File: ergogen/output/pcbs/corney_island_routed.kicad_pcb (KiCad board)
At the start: 2 copper layers, 134.2 x 92.7 mm, 46 parts

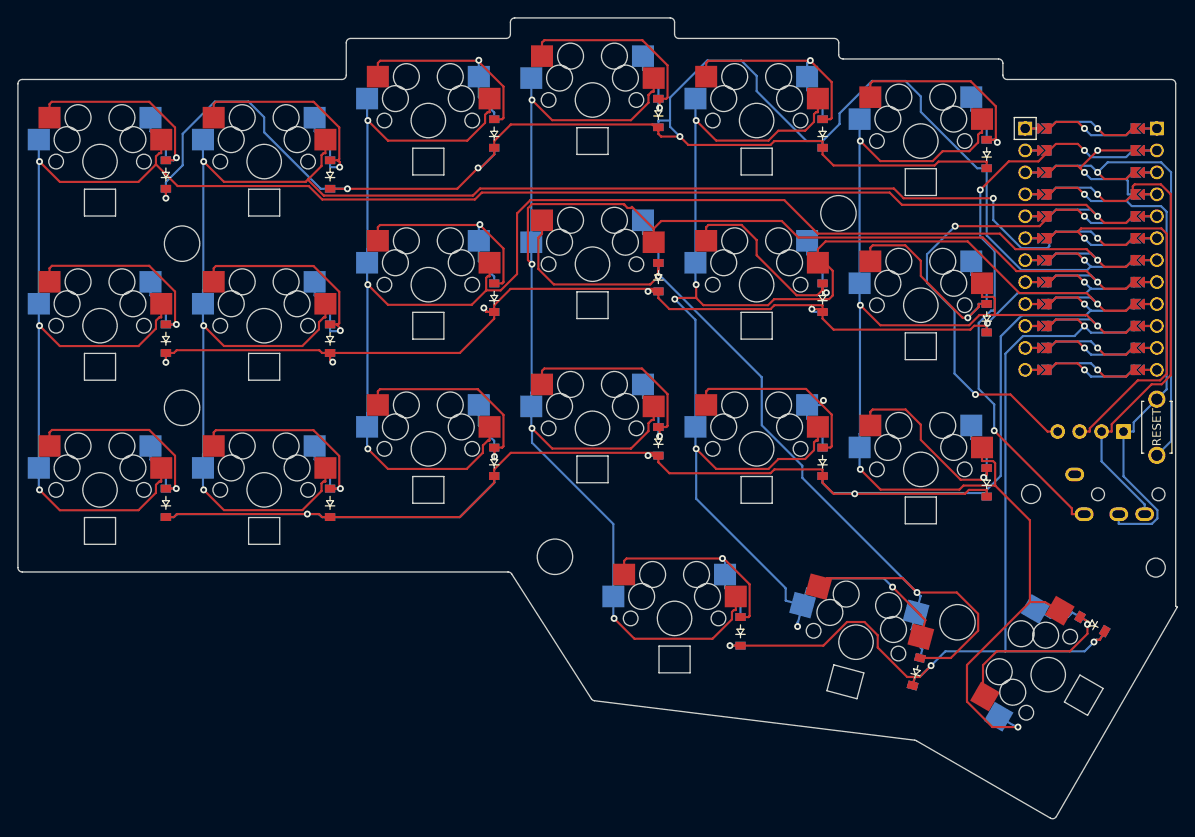
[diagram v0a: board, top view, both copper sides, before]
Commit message: Add per-key reversible LEDs
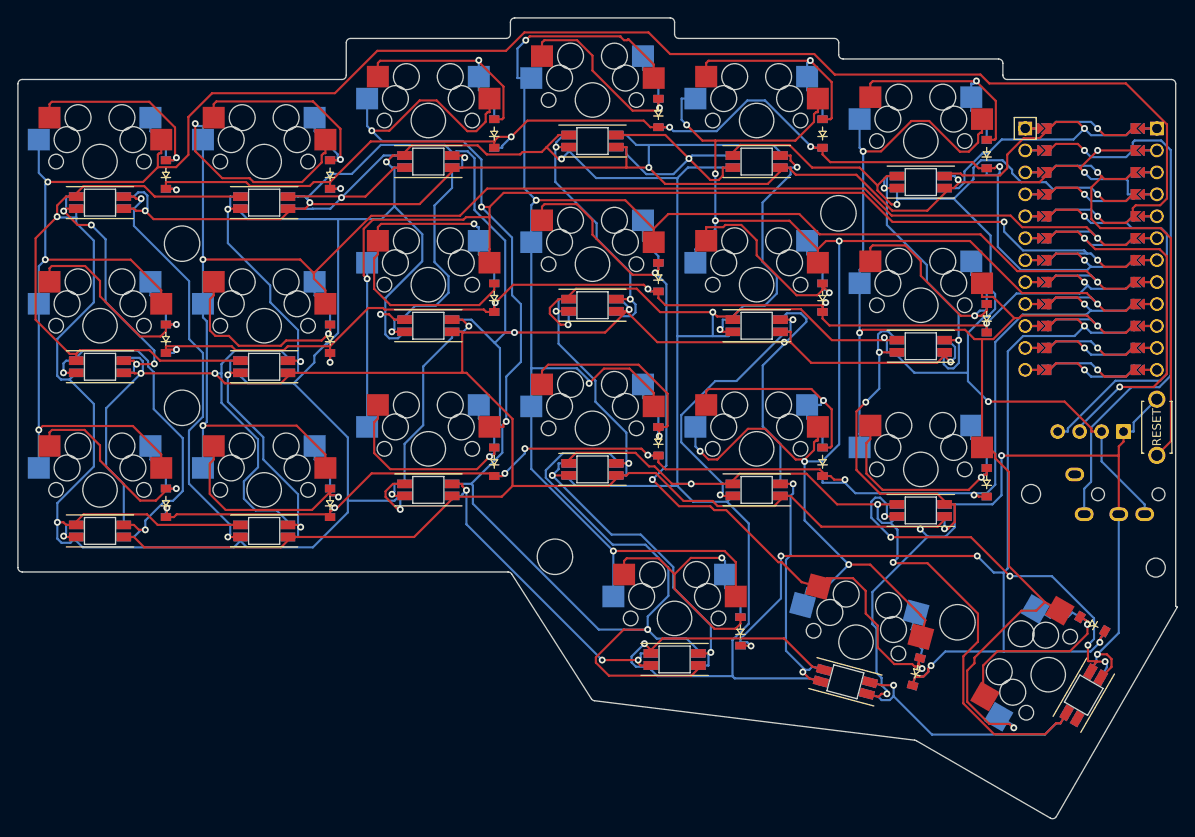
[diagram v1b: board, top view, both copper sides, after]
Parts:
- added LED1: YS-SK6812MINI-E, YS-SK6812MINI-E, F.Cu at (100.0, 104.8)
- added LED10: YS-SK6812MINI-E, YS-SK6812MINI-E, F.Cu at (157.0, 97.6)
- added LED11: YS-SK6812MINI-E, YS-SK6812MINI-E, F.Cu at (157.0, 78.6)
- added LED12: YS-SK6812MINI-E, YS-SK6812MINI-E, F.Cu at (157.0, 59.6)
- added LED13: YS-SK6812MINI-E, YS-SK6812MINI-E, F.Cu at (176.0, 100.0)
- added LED14: YS-SK6812MINI-E, YS-SK6812MINI-E, F.Cu at (176.0, 81.0)
- added LED15: YS-SK6812MINI-E, YS-SK6812MINI-E, F.Cu at (176.0, 62.0)
- added LED16: YS-SK6812MINI-E, YS-SK6812MINI-E, F.Cu at (195.0, 102.4)
- added LED17: YS-SK6812MINI-E, YS-SK6812MINI-E, F.Cu at (195.0, 83.4)
- added LED18: YS-SK6812MINI-E, YS-SK6812MINI-E, F.Cu at (195.0, 64.4)
- added LED19: YS-SK6812MINI-E, YS-SK6812MINI-E, F.Cu at (166.5, 119.6)
- added LED2: YS-SK6812MINI-E, YS-SK6812MINI-E, F.Cu at (100.0, 85.8)
- added LED20: YS-SK6812MINI-E, YS-SK6812MINI-E, F.Cu at (186.3, 122.2)
- added LED21: YS-SK6812MINI-E, YS-SK6812MINI-E, F.Cu at (213.9, 123.8)
- added LED3: YS-SK6812MINI-E, YS-SK6812MINI-E, F.Cu at (100.0, 66.8)
- added LED4: YS-SK6812MINI-E, YS-SK6812MINI-E, F.Cu at (119.0, 104.8)
- added LED5: YS-SK6812MINI-E, YS-SK6812MINI-E, F.Cu at (119.0, 85.8)
- added LED6: YS-SK6812MINI-E, YS-SK6812MINI-E, F.Cu at (119.0, 66.8)
- added LED7: YS-SK6812MINI-E, YS-SK6812MINI-E, F.Cu at (138.0, 100.0)
- added LED8: YS-SK6812MINI-E, YS-SK6812MINI-E, F.Cu at (138.0, 81.0)
- added LED9: YS-SK6812MINI-E, YS-SK6812MINI-E, F.Cu at (138.0, 62.0)
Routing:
- net GND: track 83.3 -> 773.9 mm, vias 3 -> 18
- net VCC: track 60.6 -> 737.1 mm, vias 1 -> 16
- net R0: track 216.1 -> 153.0 mm, vias 5 -> 7
- net R2: track 209.9 -> 156.7 mm, vias 4 -> 8
- net LED_18: track 0.00 -> 51.5 mm, vias 0 -> 2
- net LED_3: track 0.00 -> 49.7 mm, vias 0 -> 5
- net LED_20: track 0.00 -> 42.8 mm, vias 0 -> 2
- net LED_2: track 0.00 -> 39.9 mm, vias 0 -> 3
- net LED_11: track 0.00 -> 39.2 mm, vias 0 -> 2
- net LED_12: track 0.00 -> 38.5 mm, vias 0 -> 3
- net LED: track 11.5 -> 46.8 mm
- net LED_1: track 0.00 -> 34.5 mm, vias 0 -> 2
- net LED_6: track 0.00 -> 34.3 mm, vias 0 -> 2
- net LED_19: track 0.00 -> 33.6 mm, vias 0 -> 4
- net LED_8: track 0.00 -> 33.0 mm, vias 0 -> 1
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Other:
- outline, holes or cut-outs redrawn

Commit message: Switch to reversible TRRS jack
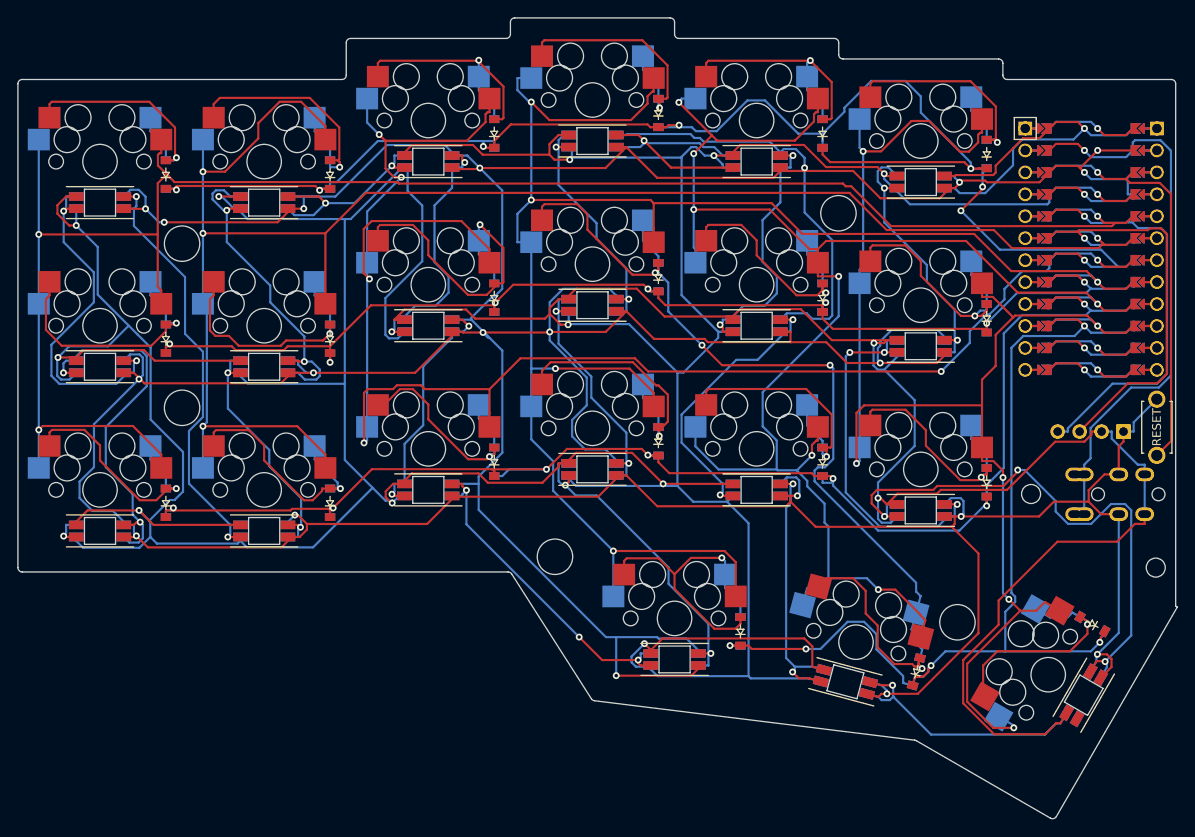
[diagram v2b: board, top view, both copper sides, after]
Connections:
- TRRS1 pad 1: J1-PadA -> data
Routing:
- net GND: track 773.9 -> 715.3 mm, vias 18 -> 21
- net C0: track 244.6 -> 212.7 mm, vias 4 -> 3
- net R0: track 153.0 -> 180.3 mm, vias 7 -> 8
- net LED_3: track 49.7 -> 66.5 mm, vias 5 -> 3
- net R3: track 128.9 -> 115.9 mm, vias 6 -> 5
- net VCC: track 737.1 -> 749.7 mm, vias 16 -> 14
- net middle_home: track 105.3 -> 117.7 mm, vias 3 -> 4
- net C2: track 204.7 -> 193.9 mm
- net LED_16: track 29.5 -> 38.4 mm
- net LED_15: track 31.1 -> 23.4 mm, vias 1 -> 2
- net R2: track 156.7 -> 164.1 mm, vias 8 -> 7
- net LED_19: track 33.6 -> 40.8 mm, vias 4 -> 2
- net C5: track 166.5 -> 173.6 mm, vias 4 -> 6
- net ring_home: track 42.7 -> 37.0 mm
- net RST: track 52.3 -> 47.8 mm
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
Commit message: Add LED and diode rotation, diode shift
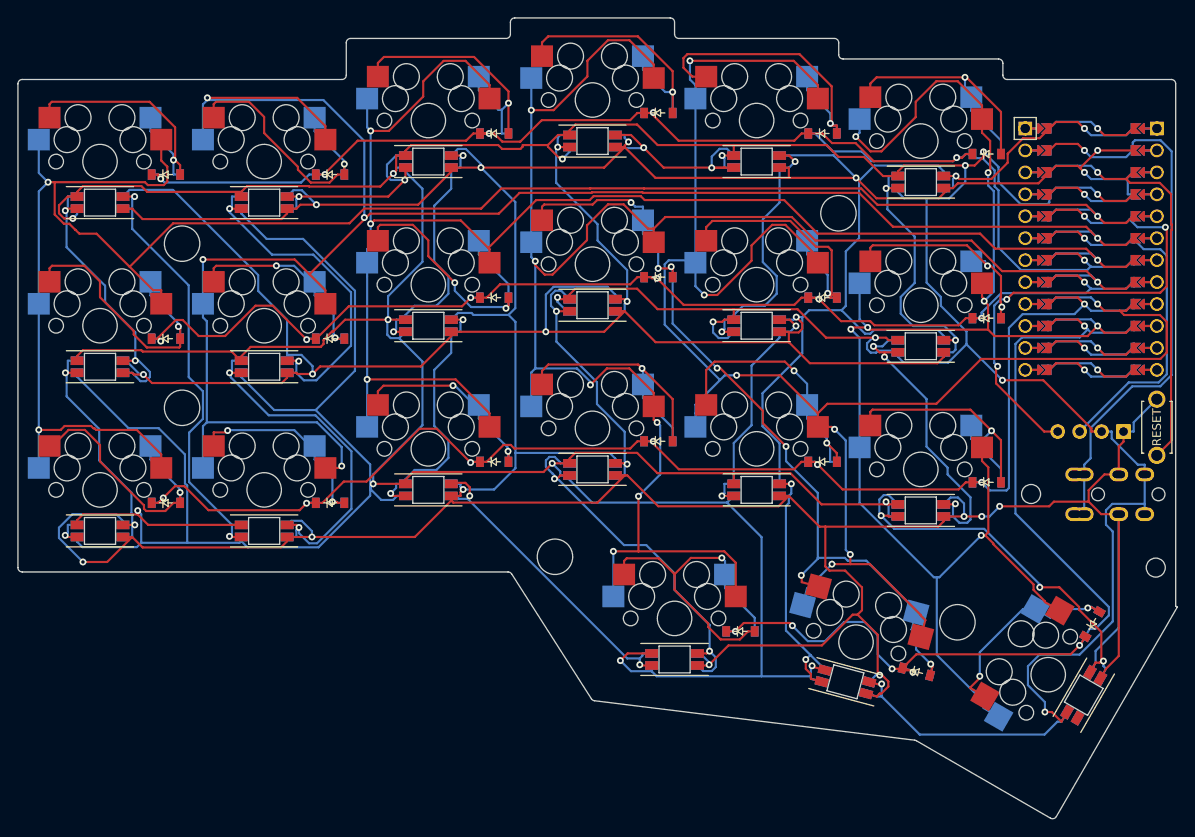
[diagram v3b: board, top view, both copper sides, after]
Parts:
- turned D1 to 0 degrees
- turned D10 to 0 degrees
- turned D11 to 0 degrees
- turned D12 to 0 degrees
- turned D13 to 0 degrees
- turned D14 to 0 degrees
- turned D15 to 0 degrees
- turned D16 to 0 degrees
- turned D17 to 0 degrees
- turned D18 to 0 degrees
- turned D19 to 0 degrees
- turned D2 to 0 degrees
- turned D20 to 345 degrees
- turned D21 to 60 degrees
- turned D3 to 0 degrees
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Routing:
- net VCC: track 749.7 -> 714.1 mm, vias 14 -> 19
- net GND: track 715.3 -> 738.9 mm, vias 21 -> 19
- net middle_home: track 117.7 -> 95.2 mm, vias 4 -> 7
- net LED_3: track 66.5 -> 46.1 mm
- net C4: track 189.9 -> 210.1 mm
- net LED: track 47.0 -> 29.5 mm, vias 1 -> 2
- net C1: track 204.8 -> 221.7 mm, vias 4 -> 5
- net R0: track 180.3 -> 164.5 mm, vias 8 -> 6
- net LED_20: track 43.2 -> 28.9 mm
- net SDA: track 48.5 -> 62.2 mm, vias 1 -> 4
- net C2: track 193.9 -> 180.5 mm, vias 6 -> 4
- net C0: track 212.7 -> 224.8 mm
- net LED_17: track 29.5 -> 41.4 mm
- net SCL: track 51.3 -> 42.8 mm
- net C5: track 173.6 -> 181.8 mm, vias 6 -> 7
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
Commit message: Fix missing diode rotation
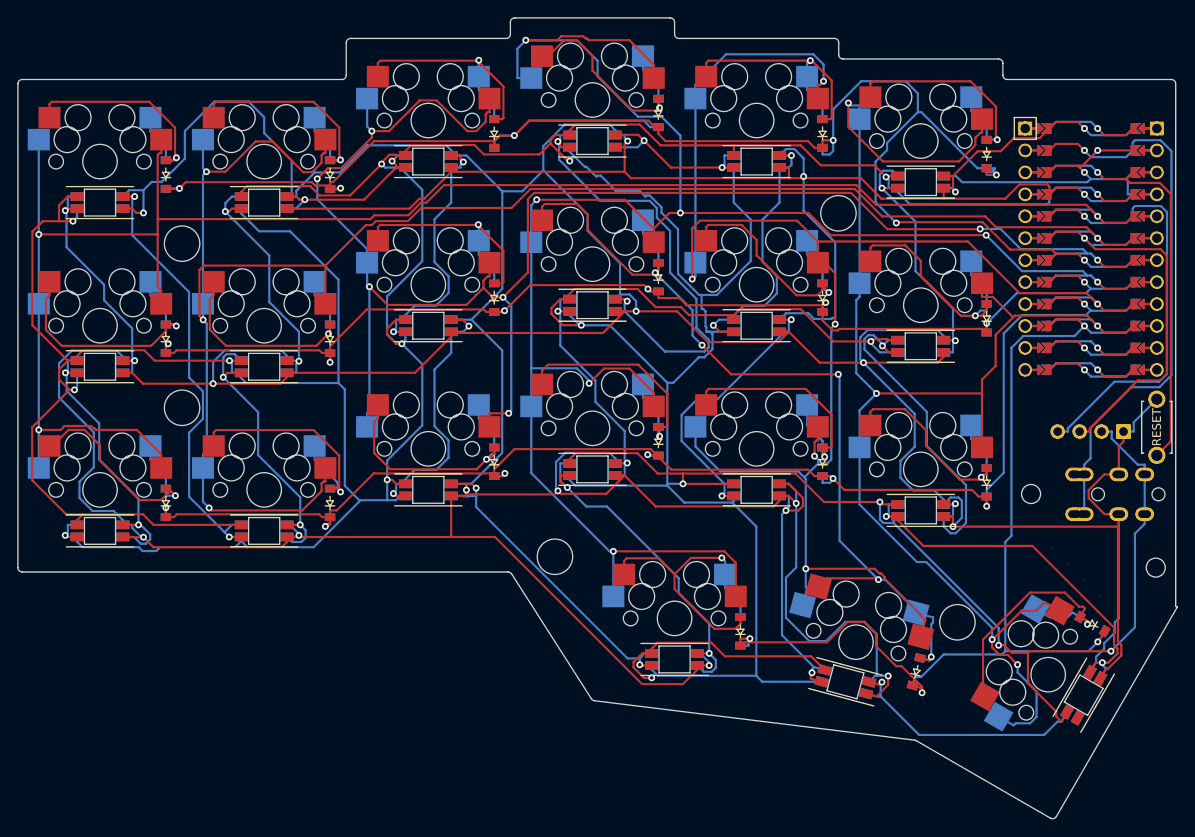
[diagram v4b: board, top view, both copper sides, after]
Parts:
- turned D1 to 90 degrees
- turned D10 to 90 degrees
- turned D11 to 90 degrees
- turned D12 to 90 degrees
- turned D13 to 90 degrees
- turned D14 to 90 degrees
- turned D15 to 90 degrees
- turned D16 to 90 degrees
- turned D17 to 90 degrees
- turned D18 to 90 degrees
- turned D19 to 90 degrees
- turned D2 to 90 degrees
- turned D20 to 75 degrees
- turned D21 to 150 degrees
- turned D3 to 90 degrees
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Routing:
- net GND: track 738.9 -> 804.5 mm, vias 19 -> 17
- net R0: track 164.5 -> 194.8 mm, vias 6 -> 7
- net VCC: track 714.1 -> 739.3 mm, vias 19 -> 16
- net LED_9: track 29.1 -> 53.9 mm
- net C3: track 207.7 -> 225.6 mm
- net C2: track 180.5 -> 194.1 mm, vias 4 -> 7
- net C0: track 224.8 -> 211.3 mm
- net C4: track 210.1 -> 197.4 mm, vias 7 -> 6
- net SDA: track 62.2 -> 50.8 mm, vias 4 -> 1
- net LED_16: track 40.7 -> 29.9 mm
- net C1: track 221.7 -> 211.9 mm, vias 5 -> 4
- net middle_home: track 95.2 -> 104.5 mm, vias 7 -> 5
- net LED_17: track 41.4 -> 33.8 mm
- net index_top: track 37.5 -> 30.4 mm
- net far_home: track 25.0 -> 31.2 mm, vias 2 -> 1
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
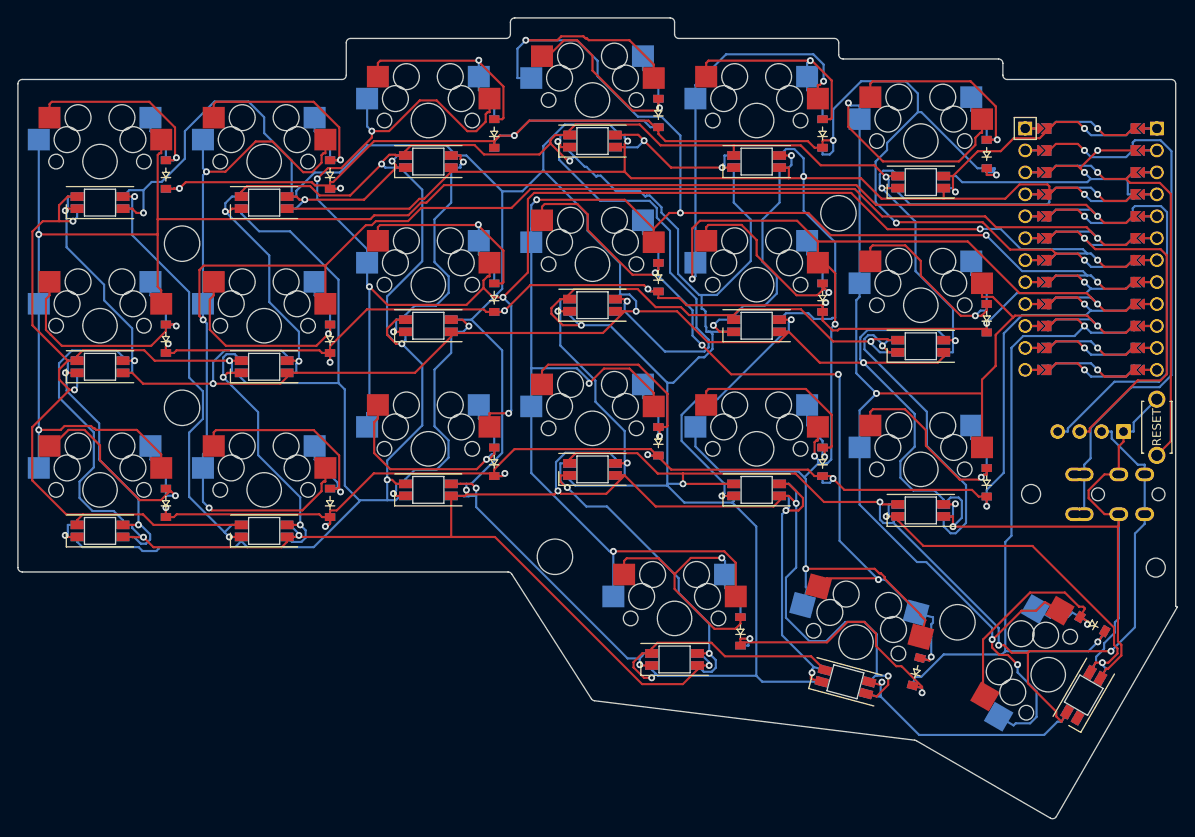
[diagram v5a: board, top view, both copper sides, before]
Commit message: Update MCU pinouts
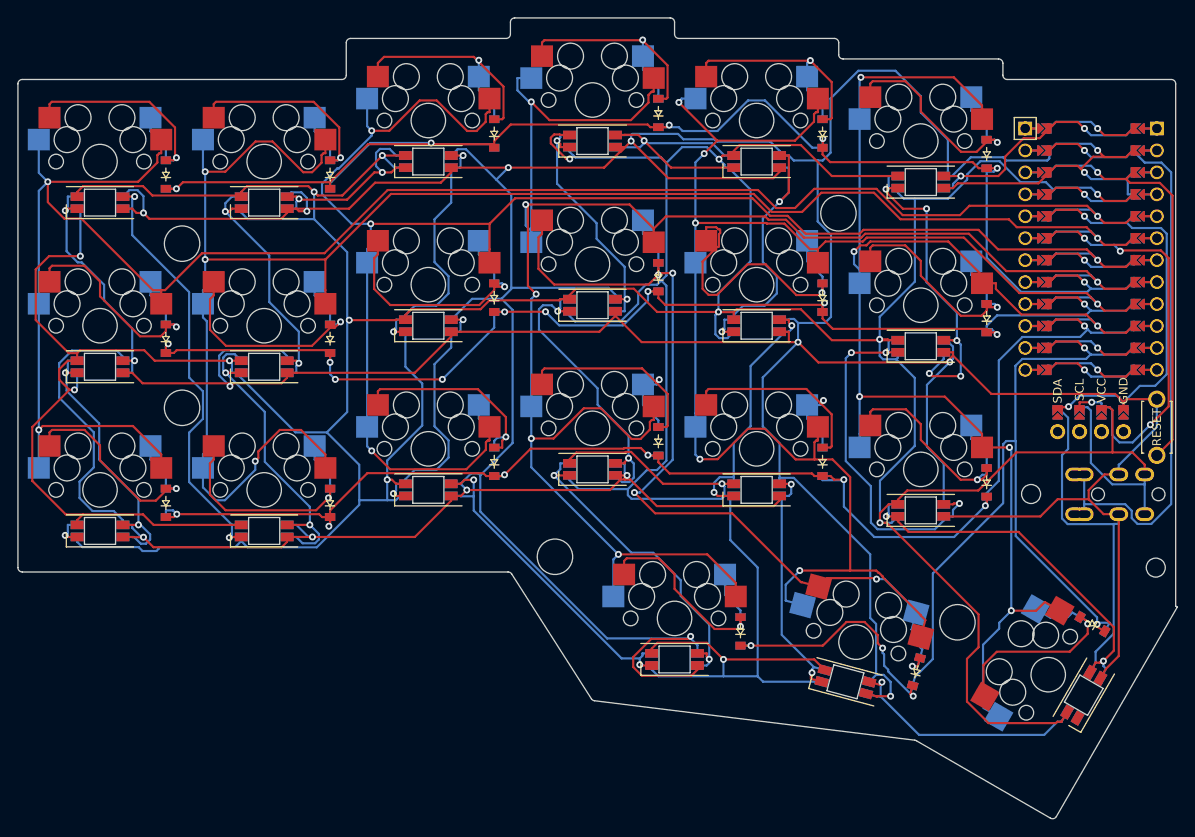
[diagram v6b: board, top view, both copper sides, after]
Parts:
- removed OLED1: OLED, lib:OLED_headers
- added LED22: combined_oled, combined_oled, F.Cu at (214.6, 91.2)
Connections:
- net P16 renamed MOSI
- MCU1 pad 14: P8 -> R3
- MCU1 pad 15: R3 -> R2
- MCU1 pad 16: R2 -> R1
- MCU1 pad 17: R1 -> R0
- MCU1 pad 18: R0 -> CS
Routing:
- net VCC: track 739.3 -> 765.4 mm, vias 16 -> 15
- net LED_9: track 53.9 -> 29.6 mm
- net R0: track 194.8 -> 170.8 mm, vias 7 -> 6
- net GND: track 804.5 -> 820.9 mm, vias 17 -> 16
- net CS: track 0.00 -> 11.5 mm, vias 0 -> 1
- net C3: track 225.6 -> 214.3 mm, vias 7 -> 6
- net P8: track 11.2 -> 0.00 mm, vias 1 -> 0
- net C0: track 211.3 -> 222.1 mm
- net C5: track 178.3 -> 167.8 mm, vias 5 -> 6
- net C4: track 197.4 -> 186.9 mm
- net LED_8: track 21.5 -> 30.1 mm, vias 2 -> 1
- net LED_1: track 31.2 -> 39.4 mm, vias 2 -> 5
- net index_home: track 28.9 -> 36.1 mm
- net near_home: track 34.6 -> 27.5 mm
- net data: track 67.5 -> 74.4 mm
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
